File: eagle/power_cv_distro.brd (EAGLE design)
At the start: 101.6 x 80 mm, 54 parts, among them U1 POWER, U10 TLV2372IP, U11 TLV2372IP, U12 TLV2372IP, U13 TLV2372IP, U2 POWER, U3 POWER, U4 POWER, U5 POWER, U6 POWER, U7 POWER, U8 POWER, U9 POWER

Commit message: power dist do-over begins
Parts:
- removed C1, C2, C3, C4: 100n, rcl:C025-025X050
- removed C5: 10u, rcl:B45181A
- removed C8: 100n, rcl:C050-024X044
- removed JP2, JP3: (no value), pinhead:1X08
- removed R1, R10, R13, R14, R2, R5, R6, R7: 1k8, rcl:0204V
- removed R11, R12, R15, R16, R17, R18, R19, R20, R21, R22, R23, R24, R25, R26, R27, R28, R29, R3, R30, R31, R32, R4, R8, R9: 1k, rcl:0207/7
- removed U$2: FB, adafruit:FB
- added D1, D10, D11, D12, D13, D14, D15, D16, D17, D18, D19, D2, D20, D21, D22, D23, D24, D3, D4, D5, D6, D7, D8, D9: 1N4148DO35-7, TR808clone:DO35-7
- added X3, X4: (no value), con-molex:22-23-2061
- U10, U11, U12, U13: value TLV2372IP -> POWER; device Texas Instruments_By_element14_Batch_1:DIP254P762X508-8 -> eurorack:POWER_16
- moved U9 82.0 mm to (85.1, 40.0), turned to 0 degrees
- moved U11 69.2 mm to (5.08, 27.9), turned to 270 degrees
- moved U13 61.5 mm to (68.6, 27.9), turned to 270 degrees
- moved U10 46.5 mm to (55.9, 27.9), turned to 270 degrees
- moved U12 45.4 mm to (17.8, 27.9), turned to 270 degrees
- moved U7 42.5 mm to (5.08, 53.3)
- moved U3 40.9 mm to (17.8, 53.3)
- moved U2 39.9 mm to (30.5, 53.3)
- moved U1 38.9 mm to (43.2, 53.3)
- moved U6 37.9 mm to (55.9, 53.3)
- moved U5 36.4 mm to (68.6, 53.3)
- moved U8 26.1 mm to (43.2, 27.9), turned to 270 degrees
- moved U4 2.29 mm to (30.5, 27.9), turned to 270 degrees
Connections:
- removed net N$37: R22.1, U1.15, U1.16
- removed net N$38: R21.1, U1.13, U1.14
- removed net N$39: R23.1, U2.15, U2.16
- removed net N$40: R24.1, U2.13, U2.14
- removed net N$41: R25.1, U3.15, U3.16
- removed net N$42: R26.1, U3.13, U3.14
- removed net N$43: R27.1, U7.15, U7.16
- removed net N$44: R28.1, U7.13, U7.14
- removed net N$45: R29.1, U4.15, U4.16
- removed net N$46: R30.1, U4.13, U4.14
- removed net N$47: R31.1, U8.15, U8.16
- removed net N$48: R32.1, U8.13, U8.14
- removed net VDD: C1.1, C2.1, C3.1, C4.1, C5.+, C8.1, U$2.P$2, U10.8, U11.8, U12.8, U13.8
- net +12V: no longer U$2.P$1
- net +5V: now also D10.A, D11.A, D12.A, D19.A, D20.A, D21.A, D22.A, D23.A, D24.A, D7.A, D8.A, D9.A, U10.11, U10.12, U11.11, U11.12, U12.11, U12.12, U13.11, U13.12
- net -12V: now also U10.1, U10.2, U11.1, U11.2, U12.1, U12.2, U13.1, U13.2
- net GND: now also U10.3, U10.5, U10.6, U10.7, U10.8, U11.3, U11.5, U11.6, U11.7, U11.8, U12.3, U12.5, U12.6, U12.7, U12.8, U13.3, U13.5, U13.6, U13.7, U13.8; no longer C1.2, C2.2, C3.2, C4.2, C5.-, C8.2, R11.1, R12.1, R15.1, R16.1, R3.1, R4.1, R8.1, R9.1
- net N$1: now also D1.A, X3.1; no longer JP2.8, R17.2
- net N$10: now also D4.C, U2.13, U2.14; no longer JP3.7, U12.3
- net N$11: now also D5.C, U3.13, U3.14; no longer JP3.6, R27.2
- net N$12: now also D6.C, U7.13, U7.14; no longer JP3.5, U12.5
- net N$13: now also D7.C, U5.15, U5.16; no longer JP3.4, R29.2
- net N$14: now also D8.C, U6.15, U6.16; no longer R10.2, R28.2, U12.7
- net N$15: now also D9.C, U1.15, U1.16; no longer JP3.2, R31.2
- net N$16: now also D10.C, U2.15, U2.16; no longer JP3.1, U13.5
- net N$17: now also D11.C, U3.15, U3.16; no longer R1.2, R20.2, U10.7
- net N$18: now also D12.C, U7.15, U7.16; no longer R18.2, R2.2, U10.1
- net N$19: now also D13.A, X4.1; no longer R1.1, R3.2, U10.6
- net N$2: now also D2.A, X3.2; no longer JP2.7, U10.3
- net N$20: now also D14.A, X4.2; no longer R2.1, R4.2, U10.2
- net N$21: now also D15.A, X4.3; no longer R11.2, R7.1, U12.2
- net N$22: now also D17.A, X4.5; no longer R24.2, R6.2, U11.7
- net N$23: now also D18.A, X4.6; no longer R5.1, R9.2, U11.2
- net N$24: now also D16.A, X4.4; no longer R6.1, R8.2, U11.6
- net N$25: now also D13.C, U11.13, U11.14; no longer R10.1, R12.2, U12.6
- net N$26: now also D14.C, U12.13, U12.14; no longer R21.2, R5.2, U11.1
- net N$27: now also D15.C, U4.13, U4.14; no longer R26.2, R7.2, U12.1
- net N$28: now also D16.C, U8.13, U8.14; no longer R13.2, R30.2, U13.1
- net N$29: now also D17.C, U10.13, U10.14; no longer R14.2, R32.2, U13.7
- net N$3: now also D3.A, X3.3; no longer JP2.6, R19.2
- net N$30: now also D18.C, U13.13, U13.14; no longer JP3.3, U13.3
- net N$31: now also D19.C, U11.15, U11.16; no longer R13.1, R15.2, U13.2
- net N$32: now also D20.C, U12.15, U12.16; no longer R14.1, R16.2, U13.6
- net N$33: now also D21.C, U4.15, U4.16; no longer R17.1, U5.15, U5.16
- net N$34: now also D22.C, U8.15, U8.16; no longer R18.1, U5.13, U5.14
- net N$35: now also D23.C, U10.15, U10.16; no longer R20.1, U6.13, U6.14
- net N$36: now also D24.C, U13.15, U13.16; no longer R19.1, U6.15, U6.16
- net N$4: now also D4.A, X3.4; no longer JP2.5, U10.5
- net N$49: now also U10.10, U10.9, U11.10, U11.9, U12.10, U12.9, U13.10, U13.9
- net N$5: now also D5.A, X3.5; no longer JP2.4, R22.2
- net N$6: now also D6.A, X3.6; no longer JP2.3, U11.3
- net N$7: now also D1.C, U5.13, U5.14; no longer JP2.2, R23.2
- net N$8: now also D2.C, U6.13, U6.14; no longer JP2.1, U11.5
- net N$9: now also D3.C, U1.13, U1.14; no longer JP3.8, R25.2
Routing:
- net GND: track 203.8 -> 0.00 mm, vias 8 -> 0
- net VDD: track 183.9 -> 0.00 mm
- net -12V: track 117.2 -> 0.00 mm
- net N$49: track 116.2 -> 0.00 mm
- net N$25: track 9.04 -> 88.0 mm
- net N$12: track 16.0 -> 89.4 mm
- net N$26: track 5.23 -> 75.2 mm
- net N$27: track 5.23 -> 59.8 mm
- net N$11: track 24.4 -> 76.3 mm
- net +5V: track 119.9 -> 70.4 mm
- net N$10: track 16.9 -> 60.8 mm
- net N$28: track 5.38 -> 45.3 mm
- net N$1: track 29.2 -> 7.65 mm
- net N$29: track 8.77 -> 29.8 mm
- net N$8: track 13.7 -> 31.8 mm
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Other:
- board size 101.6 x 80 mm -> 101.6 x 82.5 mm

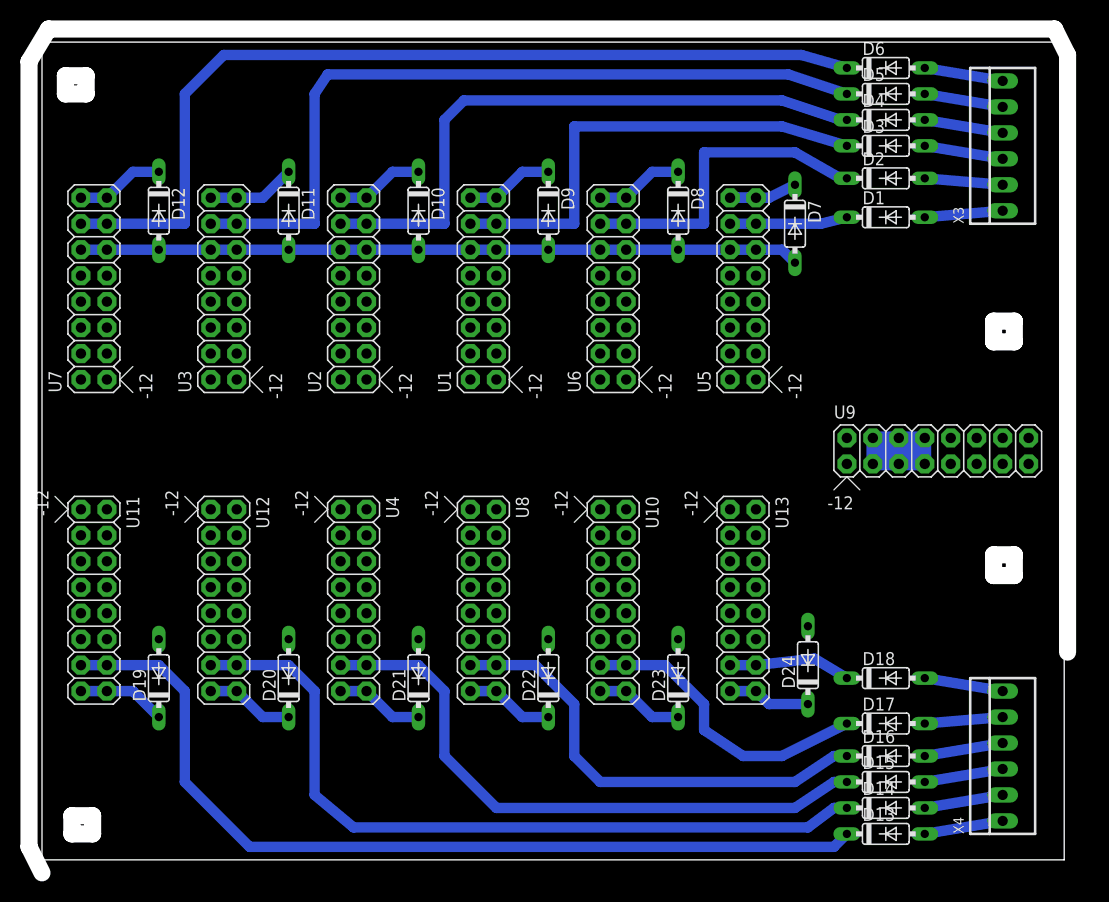
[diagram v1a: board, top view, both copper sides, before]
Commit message: power dist to six only
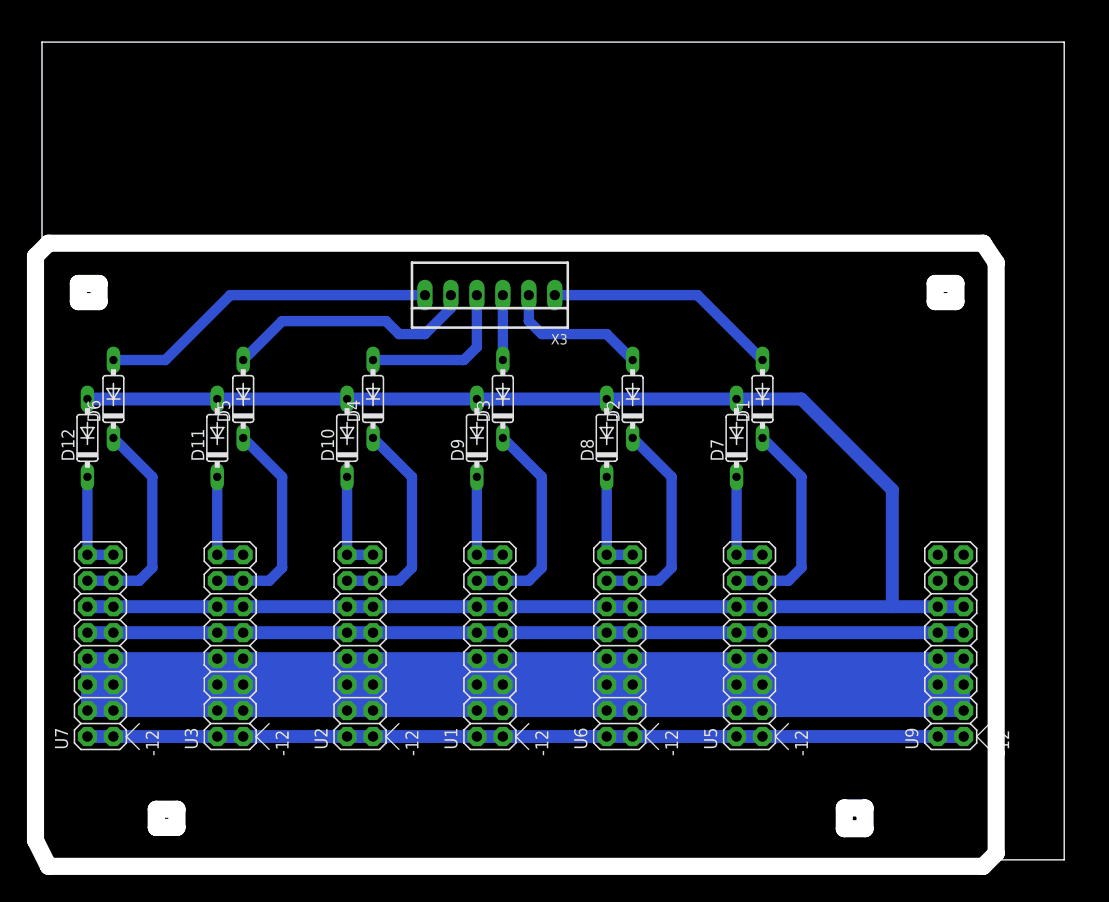
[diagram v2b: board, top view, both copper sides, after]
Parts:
- removed D13, D14, D15, D16, D17, D18, D19, D20, D21, D22, D23, D24: 1N4148DO35-7, TR808clone:DO35-7
- removed U10, U11, U12, U13, U4, U8: POWER, eurorack:POWER_16
- removed X4: (no value), con-molex:22-23-2061
- moved D6 82.2 mm to (6.99, 45.1), turned to 90 degrees
- moved D5 69.6 mm to (19.7, 45.1), turned to 90 degrees
- moved D4 57.1 mm to (32.4, 45.1), turned to 90 degrees
- moved X3 52.2 mm to (43.8, 55.2), turned to 180 degrees
- moved D3 44.9 mm to (45.1, 45.1), turned to 90 degrees
- moved U1 34.9 mm to (43.8, 18.4)
- moved U2 34.9 mm to (31.1, 18.4)
- moved U3 34.9 mm to (18.4, 18.4)
- moved U5 34.9 mm to (69.2, 18.4)
- moved U6 34.9 mm to (56.5, 18.4)
- moved U7 34.9 mm to (5.71, 18.4)
- moved D2 32.9 mm to (57.8, 45.1), turned to 90 degrees
- moved D10 23.3 mm to (29.8, 41.3), turned to 90 degrees
- moved D11 23.3 mm to (17.1, 41.3), turned to 90 degrees
- moved D12 23.3 mm to (4.45, 41.3), turned to 90 degrees
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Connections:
- removed net N$19: D13.A, X4.1
- removed net N$20: D14.A, X4.2
- removed net N$21: D15.A, X4.3
- removed net N$22: D17.A, X4.5
- removed net N$23: D18.A, X4.6
- removed net N$24: D16.A, X4.4
- removed net N$25: D13.C, U11.13, U11.14
- removed net N$26: D14.C, U12.13, U12.14
- removed net N$27: D15.C, U4.13, U4.14
- removed net N$28: D16.C, U8.13, U8.14
- removed net N$29: D17.C, U10.13, U10.14
- removed net N$30: D18.C, U13.13, U13.14
- removed net N$31: D19.C, U11.15, U11.16
- removed net N$32: D20.C, U12.15, U12.16
- removed net N$33: D21.C, U4.15, U4.16
- removed net N$34: D22.C, U8.15, U8.16
- removed net N$35: D23.C, U10.15, U10.16
- removed net N$36: D24.C, U13.15, U13.16
- removed net N$49: U1.10, U1.9, U10.10, U10.9, U11.10, U11.9, U12.10, U12.9, U13.10, U13.9, U2.10, U2.9, U3.10, U3.9, U4.10, U4.9, U5.10, U5.9, U6.10, U6.9, U7.10, U7.9, U8.10, U8.9
- net +12V: now also U1.10, U1.9, U2.10, U2.9, U3.10, U3.9, U5.10, U5.9, U6.10, U6.9, U7.10, U7.9
- net +5V: no longer D19.A, D20.A, D21.A, D22.A, D23.A, D24.A, U10.11, U10.12, U11.11, U11.12, U12.11, U12.12, U13.11, U13.12, U4.11, U4.12, U8.11, U8.12
- net -12V: no longer U10.1, U10.2, U11.1, U11.2, U12.1, U12.2, U13.1, U13.2, U4.1, U4.2, U8.1, U8.2
- net GND: no longer U10.3, U10.4, U10.5, U10.6, U10.7, U10.8, U11.3, U11.4, U11.5, U11.6, U11.7, U11.8, U12.3, U12.4, U12.5, U12.6, U12.7, U12.8, U13.3, U13.4, U13.5, U13.6, U13.7, U13.8, U4.3, U4.4, U4.5, U4.6, U4.7, U4.8, U8.3, U8.4, U8.5, U8.6, U8.7, U8.8
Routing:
- net N$25: track 88.0 -> 0.00 mm
- net N$26: track 75.2 -> 0.00 mm
- net N$12: track 89.4 -> 21.2 mm
- net N$27: track 59.8 -> 0.00 mm
- net N$11: track 76.3 -> 21.2 mm
- net N$28: track 45.3 -> 0.00 mm
- net N$10: track 60.8 -> 21.2 mm
- net N$29: track 29.8 -> 0.00 mm
- net +5V: track 70.4 -> 98.3 mm
- net N$9: track 47.3 -> 21.2 mm
- net N$6: track 7.73 -> 33.1 mm
- net N$5: track 7.73 -> 24.7 mm
- net N$1: track 7.65 -> 23.0 mm
- net N$30: track 12.0 -> 0.00 mm
- net N$8: track 31.8 -> 21.2 mm
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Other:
- board size 101.6 x 82.5 mm -> 100.6 x 80.6 mm

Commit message: added layout png
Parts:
- moved U9 12.7 mm to (76.2, 18.4)
- moved U5 7.62 mm to (61.6, 18.4)
- moved D1 7.62 mm to (62.9, 45.1)
- moved D7 7.62 mm to (60.3, 41.3)
- moved U6 6.35 mm to (50.2, 18.4)
- moved D2 6.35 mm to (51.4, 45.1)
- moved D8 6.35 mm to (48.9, 41.3)
- moved D3 5.08 mm to (40.0, 45.1)
- moved D9 5.08 mm to (37.5, 41.3)
- moved U1 5.08 mm to (38.7, 18.4)
- moved X3 5.08 mm to (38.7, 55.2)
- moved D10 3.81 mm to (26.0, 41.3)
- moved D4 3.81 mm to (28.6, 45.1)
- moved U2 3.81 mm to (27.3, 18.4)
- moved D11 2.54 mm to (14.6, 41.3)
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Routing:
- net +5V: track 98.3 -> 90.0 mm
- net N$6: track 33.1 -> 29.7 mm
- net N$5: track 24.7 -> 22.2 mm
- net N$1: track 23.0 -> 20.4 mm
- net N$4: track 15.8 -> 14.5 mm
- net N$2: track 14.3 -> 13.0 mm
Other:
- outline, holes or cut-outs redrawn
